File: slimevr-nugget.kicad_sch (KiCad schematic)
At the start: 0 parts

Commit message: Base design for nRF52840-QFAA
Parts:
- added AE1: Antenna, symbol Device:Antenna
- added C1, C2, C3, C4: 12pF, symbol Device:C
- added C10, C11, C12, C13, C14: 100nF, symbol Device:C
- added C15, C8: 1.0uF, symbol Device:C
- added C5: 1.0pF, symbol Device:C
- added C6: 1.2pF, symbol Device:C
- added C7: 0.1nF, symbol Device:C
- added C9: 47nF, symbol Device:C
- added L1: 4.7nH, symbol Device:L
- added L2: 2.2nH, symbol Device:L
- added L3: 10uH, symbol Device:L
- added L4: 15nH, symbol Device:L
- added U1: nRF52840-QFXX, Package_DFN_QFN:QFN-48-1EP_6x6mm_P0.4mm_EP4.6x4.6mm_ThermalVias, symbol PCM_nordic-lib-kicad-nrf52:nRF52840-QFXX
- added Y1: 32MHz, symbol Device:Crystal_GND2
- added Y2: 32.768kHz, symbol Device:Crystal
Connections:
- new net: C6.2, L1.2, L2.1
- new net: AE1.1 (A), L2.2
- new net: C7.2, U1.34 (DEC3)
- new net: C10.2, U1.1 (DEC1)
- new net: C1.2, U1.35 (XC1), Y1.1
- new net: C5.2, L1.1, U1.31 (ANT)
- new net: C4.2, U1.3 (P0.01), Y2.1
- new net: C8.2, C9.2, L4.2, U1.33 (DEC6), U1.46 (DEC4)
- new net: L3.2, L4.1
- new net: C3.2, U1.2 (P0.00), Y2.2
- new net: C2.2, U1.36 (XC2), Y1.3
- new net: L3.1, U1.47 (DCC)
- new net GND: C1.1, C10.1, C11.1, C12.1, C13.1, C14.1, C15.1, C2.1, C3.1, C4.1, C5.1, C6.1, C7.1, C8.1, C9.1, U1.32 (VSS_PA), U1.45 (VSS), U1.49 (VSS), Y1.2
- new net VDD: C11.2, C12.2, C13.2, C14.2, C15.2, U1.12 (VDD), U1.17 (VDD), U1.25 (VDD), U1.37 (VDD), U1.48 (VDD)

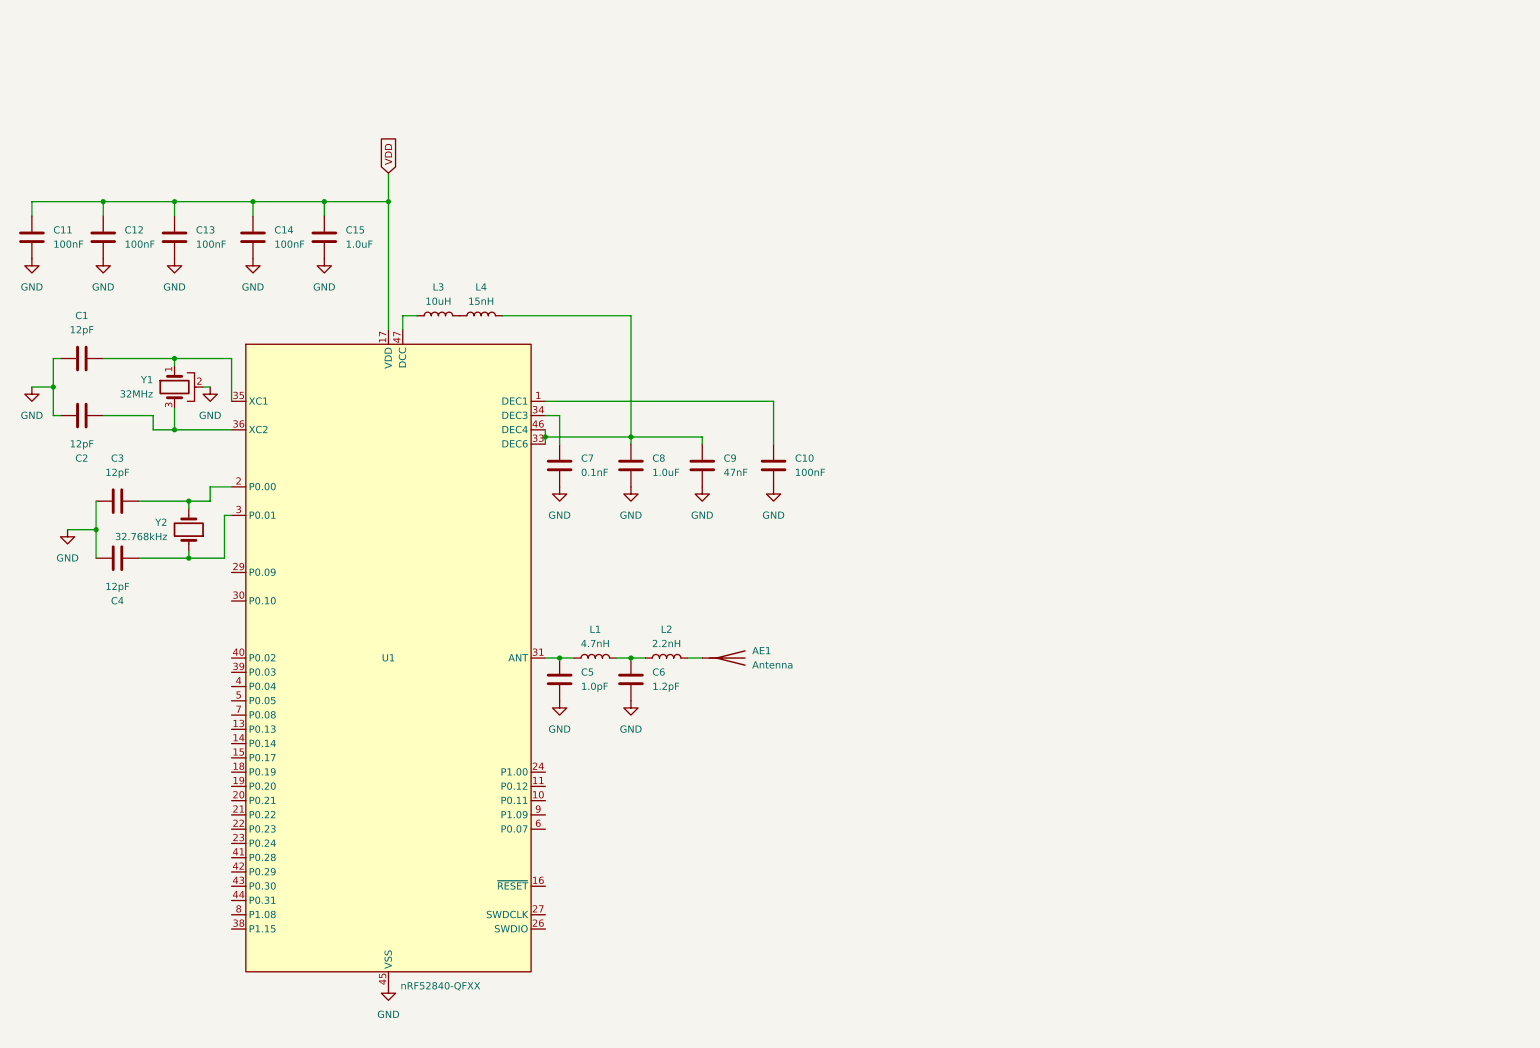
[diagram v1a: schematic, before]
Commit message: Add power path circuit
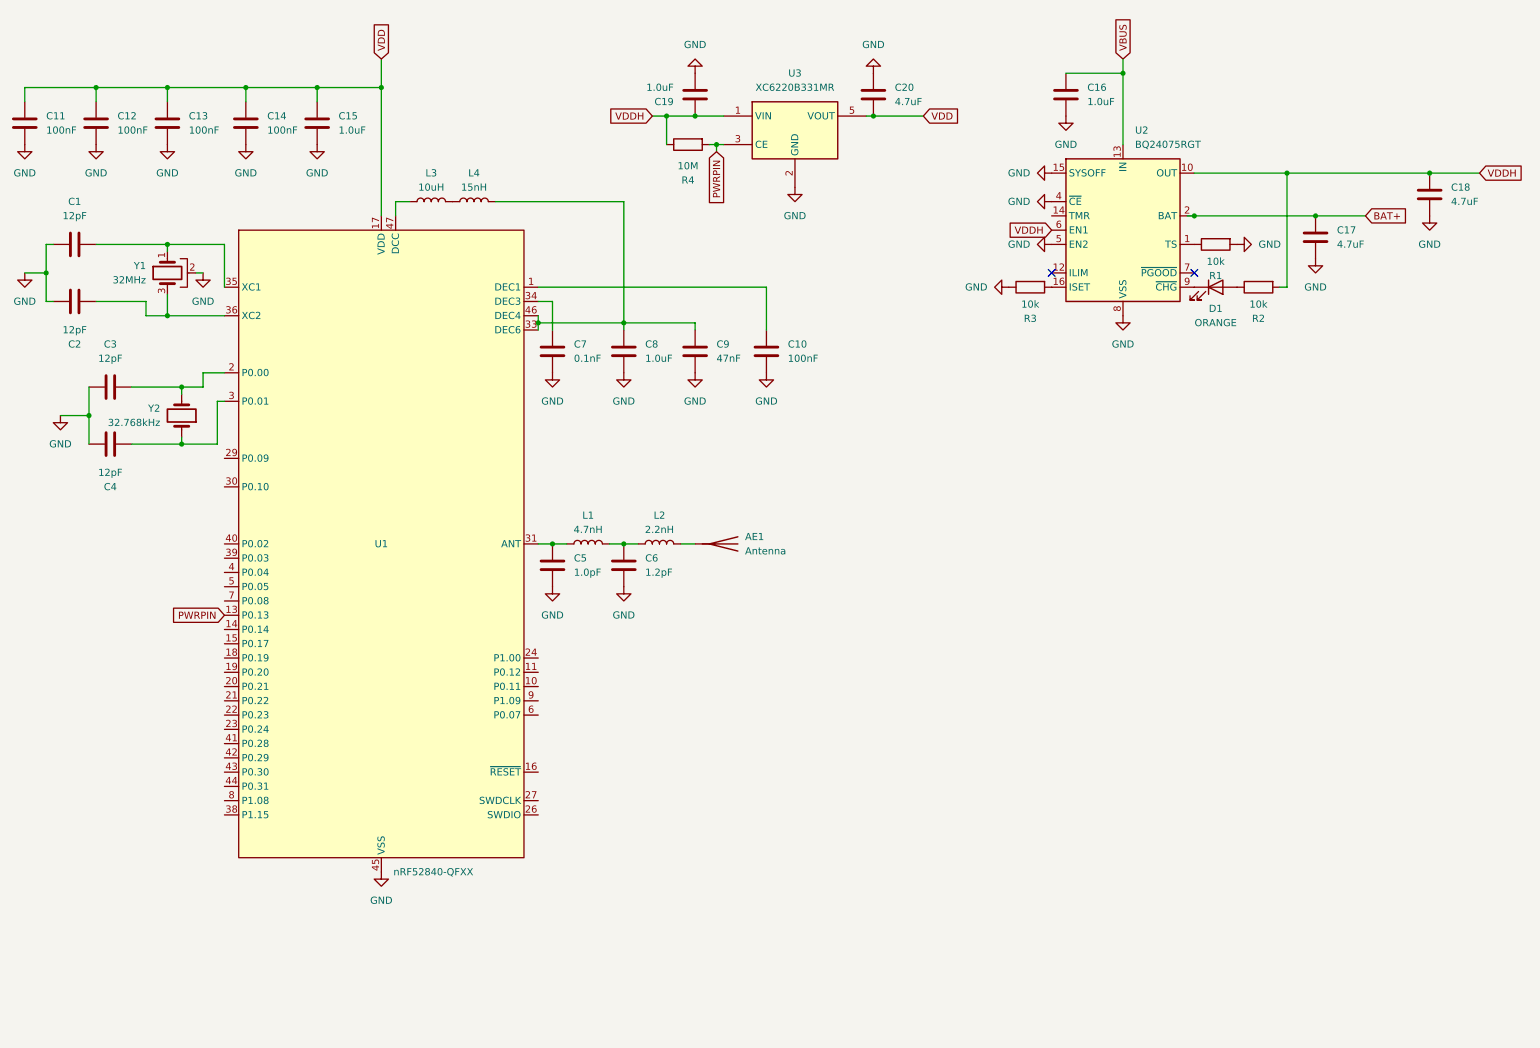
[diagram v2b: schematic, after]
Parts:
- added C16, C19: 1.0uF, symbol Device:C
- added C17, C18, C20: 4.7uF, symbol Device:C
- added D1: ORANGE, symbol Device:LED
- added R1, R2, R3: 10k, symbol Device:R
- added R4: 10M, symbol Device:R
- added U2: BQ24075RGT, Package_DFN_QFN:VQFN-16-1EP_3x3mm_P0.5mm_EP1.6x1.6mm, symbol Battery_Management:BQ24075RGT
- added U3: XC6220B331MR, Package_TO_SOT_SMD:SOT-23-5, symbol Regulator_Linear:XC6220B331MR
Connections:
- net GND: now also C16.1, C17.1, C18.1, C19.1, C20.1, R1.2, R3.1, U2.15 (SYSOFF), U2.17 (VSS), U2.4 (~{CE}), U2.5 (EN2), U2.8 (VSS), U3.2 (GND)
- net VDD: now also C20.2, U3.5 (VOUT)
- net PWRPIN: now reaches U1.13 (P0.13)
- net PWRPIN: now also R4.2, U3.3 (CE)
- new net: R1.1, U2.1 (TS)
- new net: R3.2, U2.16 (ISET)
- new net: D1.1 (K), U2.9 (~{CHG})
- new net: D1.2 (A), R2.1
- new net BAT+: C17.2, U2.2 (BAT), U2.3 (BAT)
- new net VBUS: C16.2, U2.13 (IN)
- new net VDDH: C18.2, C19.2, R2.2, R4.1, U2.10 (OUT), U2.11 (OUT), U2.6 (EN1), U3.1 (VIN)
- no-connect marks 0 -> 2
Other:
- moved on the sheet: AE1, C1, C10, C11, C12, C13, C14, C15, C2, C3, C4, C5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

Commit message: Add rest of ICs (routing unfinished)
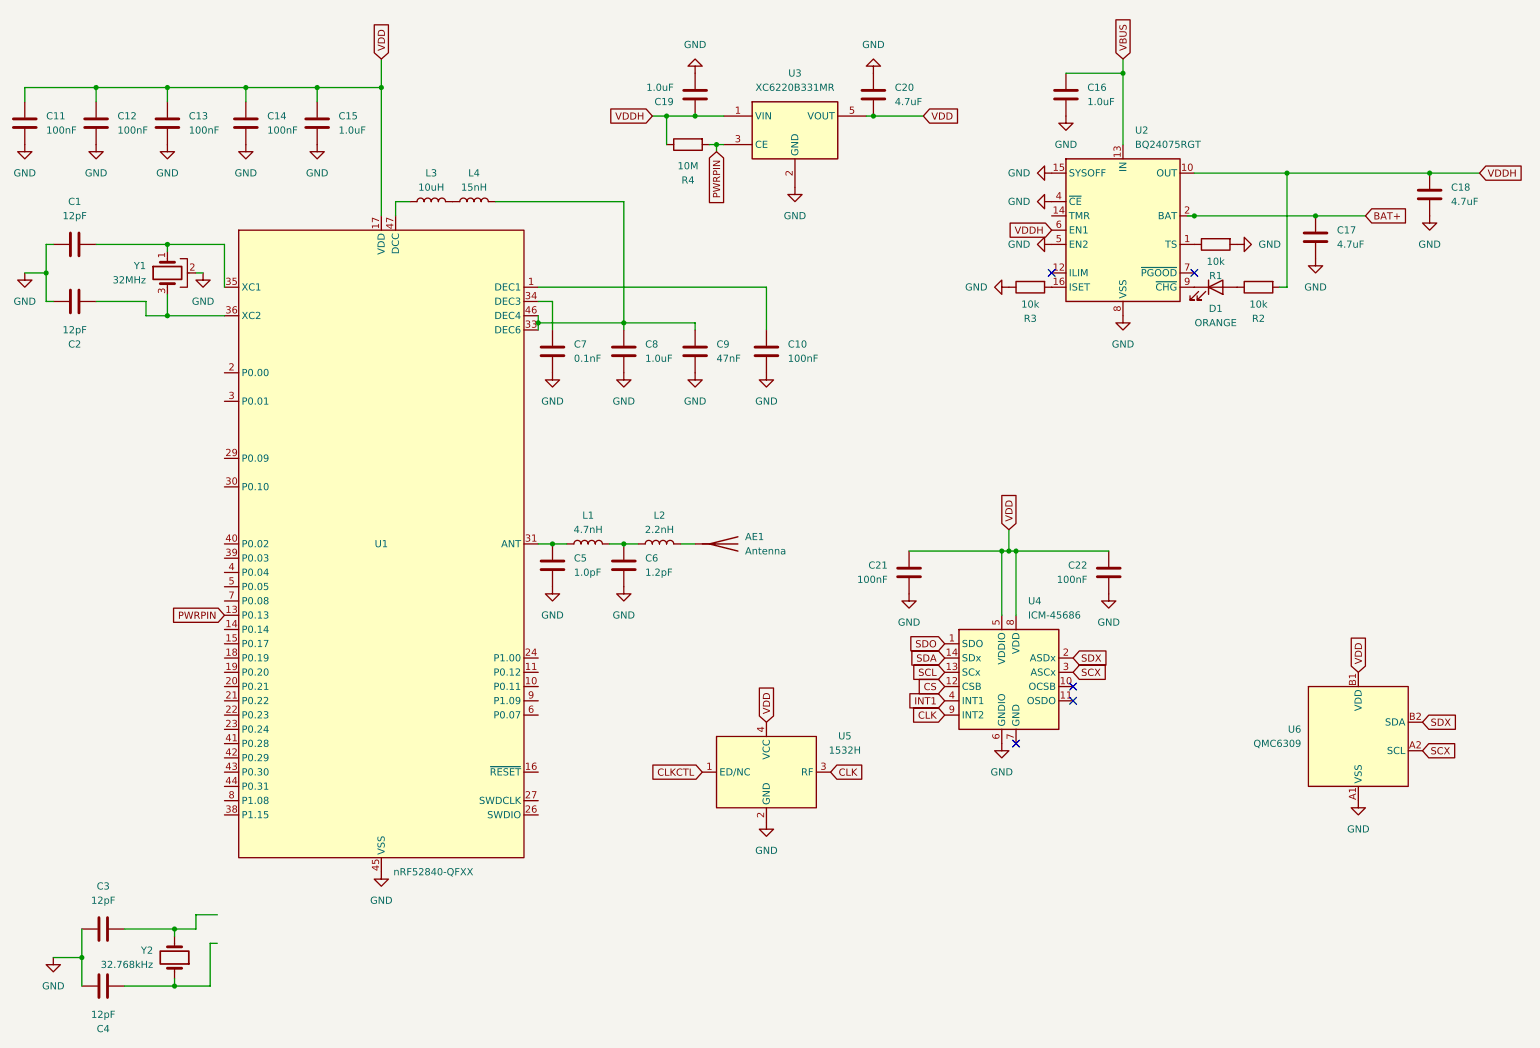
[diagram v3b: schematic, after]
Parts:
- added C21, C22: 100nF, symbol Device:C
- added U4: ICM-45686, Package_LGA:Bosch_LGA-14_3x2.5mm_P0.5mm, symbol Sensor_Motion:BMI160
- added U5: 1532H, Custom_Oscillator:Oscillator_SMD_HCI_1532H-4Pin_3.2x2.5mm, symbol Mumo Symbols:HCI_1532H
- added U6: QMC6309, symbol Mumo Symbols:QMC6309
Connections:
- net GND: now also C21.1, C22.1, U4.6 (GNDIO), U5.2 (GND), U6.A1 (VSS)
- net VDD: now also C21.2, C22.2, U4.5 (VDDIO), U4.8 (VDD), U5.4 (VCC), U6.B1 (VDD)
- net at C4.2, Y2.1: no longer U1.3 (P0.01)
- net at C3.2, Y2.2: no longer U1.2 (P0.00)
- new net CLK: U4.9 (INT2), U5.3 (RF)
- new net CLKCTL: U5.1 (ED/NC)
- new net CS: U4.12 (CSB)
- new net INT1: U4.4 (INT1)
- new net SCL: U4.13 (SCx)
- new net SCX: U4.3 (ASCx), U6.A2 (SCL)
- new net SDA: U4.14 (SDx)
- new net SDO: U4.1 (SDO)
- new net SDX: U4.2 (ASDx), U6.B2 (SDA)
- no-connect marks 2 -> 5
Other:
- moved on the sheet: C3, C4, Y2

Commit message: Complete circuit and routing
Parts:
- removed AE1: Antenna, symbol Device:Antenna
- removed Y2: 32.768kHz, symbol Device:Crystal
- added AE1: Antenna_Shield, RF_Antenna:Texas_SWRA117D_2.4GHz_Left, symbol Device:Antenna_Shield
- added C23: TODO, Capacitor_SMD:C_0402_1005Metric, symbol Device:C
- added C24: 1.0uF, Capacitor_SMD:C_0402_1005Metric, symbol Device:C
- added D2: LED, LED_SMD:LED_0402_1005Metric, symbol Device:LED
- added L5: TODO, Resistor_SMD:R_0402_1005Metric, symbol Device:L
- added R10, R11, R5, R6, R7, R8, R9: 10k, Resistor_SMD:R_0402_1005Metric, symbol Device:R
- added TP1: +5V, TestPoint:TestPoint_Pad_D1.5mm, symbol Connector:TestPoint
- added TP2: GND, TestPoint:TestPoint_Pad_D1.5mm, symbol Connector:TestPoint
- added TP3: SWC, TestPoint:TestPoint_Pad_D1.5mm, symbol Connector:TestPoint
- added TP4: SWD, TestPoint:TestPoint_Pad_D1.5mm, symbol Connector:TestPoint
- C1, C10, C11, C12, C13, C14, C15, C16, C17, C18, C19, C2, C20, C21, C22, C5, C6, C7, C8, C9: footprint (none) -> Capacitor_SMD:C_0402_1005Metric
- C3: value 12pF -> 2.2uF; footprint (none) -> Capacitor_SMD:C_0402_1005Metric
- C4: value 12pF -> TODO; footprint (none) -> Capacitor_SMD:C_0402_1005Metric; now not fitted
- D1: footprint (none) -> LED_SMD:LED_0402_1005Metric
- L1, L2, L3, L4: footprint (none) -> Inductor_SMD:L_0402_1005Metric
- R1, R2, R3, R4: footprint (none) -> Resistor_SMD:R_0402_1005Metric
- U5: footprint Custom_Oscillator:Oscillator_SMD_HCI_1532H-4Pin_3.2x2.5mm -> Crystal:Crystal_SMD_3225-4Pin_3.2x2.5mm
- U6: footprint (none) -> Mumo Footprints:QMC6309
- Y1: footprint (none) -> Crystal:Crystal_SMD_3225-4Pin_3.2x2.5mm; symbol Device:Crystal_GND2 -> Device:Crystal_GND24
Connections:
- net CLK: now also U1.2 (P0.00)
- net CS: now also U1.18 (P0.19), R8.2
- net GND: now also C3.2, U1.3 (P0.01), Y1.4 (G), AE1.2 (Shield), C23.1, C24.1, R11.2, TP2.1; no longer C3.1
- net SCL: now also U1.20 (P0.21), R7.2
- net SCX: now also R10.2
- net SDA: now also U1.21 (P0.22), R6.2
- net SDO: now also U1.22 (P0.23), R5.2
- net SDX: now also R9.2
- net VBUS: now also TP1.1
- net VDD: now also C3.1, C24.2, R10.1, R5.1, R6.1, R7.1, R8.1, R9.1
- net at L2.2: now also C4.2, L5.1
- net SWD: now reaches U1.26 (SWDIO)
- net SWD: now also TP4.1
- net SWC: now reaches U1.27 (SWDCLK)
- net SWC: now also TP3.1
- net CLKCTL: no longer names the net of U5.1 (ED/NC)
- new net: AE1.1 (A), C23.2, L5.2
- new net: D2.1 (K), R11.1
- no-connect marks 5 -> 6
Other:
- moved on the sheet: C21, C22, U4, U5, U6

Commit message: Revision 2
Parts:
- removed D1: ORANGE, LED_SMD:LED_0402_1005Metric, symbol Device:LED
- removed D2: LED, LED_SMD:LED_0402_1005Metric, symbol Device:LED
- removed U2: BQ24075RGT, Package_DFN_QFN:VQFN-16-1EP_3x3mm_P0.5mm_EP1.6x1.6mm, symbol Battery_Management:BQ24075RGT
- added R12: 10k, Resistor_SMD:R_0402_1005Metric, symbol Device:R
- added TP5: GND, TestPoint:TestPoint_Pad_D1.0mm, symbol Connector:TestPoint
- added TP6: BAT+, TestPoint:TestPoint_Pad_D1.0mm, symbol Connector:TestPoint
- added TP7: CHRG, TestPoint:TestPoint_Pad_D1.5mm, symbol Connector:TestPoint
- added U7: BQ24073RGT, Package_DFN_QFN:VQFN-16-1EP_3x3mm_P0.5mm_EP1.6x1.6mm, symbol Battery_Management:BQ24073RGT
- C24: value 1.0uF -> 100nF
- R4: value 10M -> 10k
- U4: value ICM-45686 -> LSM6DSV
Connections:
- net BAT+: now also TP6.1, U7.2 (BAT), U7.3 (BAT)
- net CLK: no longer U4.9 (INT2)
- net GND: now also R11.1, R4.1, U4.7 (GND), R12.1, TP5.1, U7.15 (TD), U7.17 (VSS), U7.4 (~{CE}), U7.5 (EN2), U7.6 (EN1), U7.8 (VSS); no longer R11.2, R3.1
- net INT1: now also U1.23 (P0.24)
- net VBUS: now also R2.2, U7.13 (IN)
- net VDDH: now also U3.3 (CE), U7.10 (OUT), U7.11 (OUT); no longer R2.2, R4.1
- net at R1.1: now also U7.1 (TS)
- net at R3.2: now also U7.16 (ISET)
- net CHG: now reaches R2.1
- net CHG: now also TP7.1, U7.9 (~{CHG})
- removed net PWRPIN: R4.2, U1.13 (P0.13), U3.3 (CE)
- new net: R3.1, R4.2
- new net: R11.2, R12.2, U7.12 (ILIM)
- no-connect marks 6 -> 29
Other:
- moved on the sheet: R2
